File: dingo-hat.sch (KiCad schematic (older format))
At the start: 51 parts, among them J1 6-13V, J14 NEOPIXEL, J15 MPU-9250, J16 4, J17 5, J18 6, J19 7, J2 Raspberry_Pi_2_3, J24 3mm_Mount, J25 3mm_Mount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

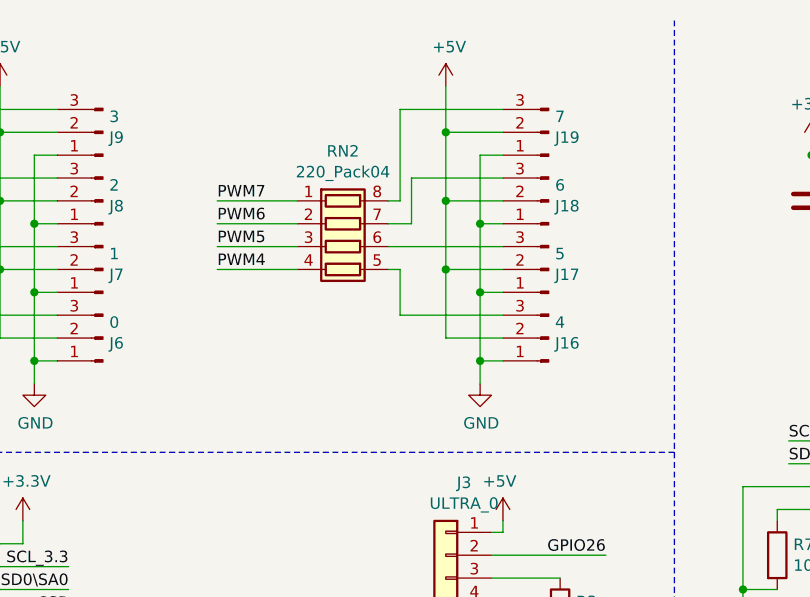
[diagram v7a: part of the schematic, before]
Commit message: Removed 4 of the Servo pins
We only need 4.
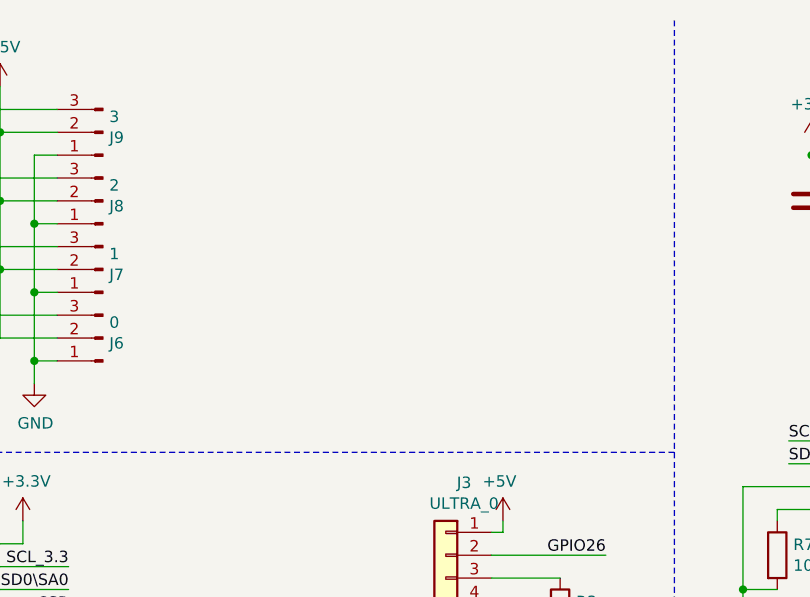
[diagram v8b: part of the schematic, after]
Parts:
- removed J16: 4, Connector_PinHeader_2.54mm:PinHeader_1x03_P2.54mm_Vertical, symbol Connector:Conn_01x03_Male
- removed J17: 5, Connector_PinHeader_2.54mm:PinHeader_1x03_P2.54mm_Vertical, symbol Connector:Conn_01x03_Male
- removed J18: 6, Connector_PinHeader_2.54mm:PinHeader_1x03_P2.54mm_Vertical, symbol Connector:Conn_01x03_Male
- removed J19: 7, Connector_PinHeader_2.54mm:PinHeader_1x03_P2.54mm_Vertical, symbol Connector:Conn_01x03_Male
- removed RN2: 220_Pack04, Resistor_SMD:R_Array_Convex_4x0603, symbol Device:R_Pack04
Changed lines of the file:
@@
 EESchema Schematic File Version 4
 LIBS:dingo-hat-cache
-EELAYER 30 0
+EELAYER 29 0
 EELAYER END
 $Descr A4 11693 8268
@@
 	5350 1000 5350 1300
 $Comp
-L Connector:Conn_01x03_Male J16
-U 1 1 5C067B2F
-P 7750 1900
-F 0 "J16" H 7722 1923 50  0000 R CNN
-F 1 "4" H 7722 1832 50  0000 R CNN
-F 2 "Connector_PinHeader_2.54mm:PinHeader_1x03_P2.54mm_Vertical" H 7750 1900 50  0001 C CNN
-F 3 "~" H 7750 1900 50  0001 C CNN
-	1    7750 1900
-	-1   0    0    1
-$EndComp
-$Comp
-L Device:R_Pack04 RN2
-U 1 1 5C067B35
-P 6850 1500
-F 0 "RN2" V 6433 1500 50  0000 C CNN
-F 1 "220_Pack04" V 6524 1500 50  0000 C CNN
-F 2 "Resistor_SMD:R_Array_Convex_4x0603" V 7125 1500 50  0001 C CNN
-F 3 "~" H 6850 1500 50  0001 C CNN
-F 4 "SMD" H 0   0   50  0001 C CNN "Package"
-	1    6850 1500
-	0    1    1    0
-$EndComp
-$Comp
-L Connector:Conn_01x03_Male J17
-U 1 1 5C067B3B
-P 7750 1600
-F 0 "J17" H 7722 1623 50  0000 R CNN
-F 1 "5" H 7722 1532 50  0000 R CNN
-F 2 "Connector_PinHeader_2.54mm:PinHeader_1x03_P2.54mm_Vertical" H 7750 1600 50  0001 C CNN
-F 3 "~" H 7750 1600 50  0001 C CNN
-	1    7750 1600
-	-1   0    0    1
-$EndComp
-$Comp
-L Connector:Conn_01x03_Male J18
-U 1 1 5C067B41
-P 7750 1300
-F 0 "J18" H 7722 1323 50  0000 R CNN
-F 1 "6" H 7722 1232 50  0000 R CNN
-F 2 "Connector_PinHeader_2.54mm:PinHeader_1x03_P2.54mm_Vertical" H 7750 1300 50  0001 C CNN
-F 3 "~" H 7750 1300 50  0001 C CNN
-	1    7750 1300
-	-1   0    0    1
-$EndComp
-$Comp
-L Connector:Conn_01x03_Male J19
-U 1 1 5C067B47
-P 7750 1000
-F 0 "J19" H 7722 1023 50  0000 R CNN
-F 1 "7" H 7722 932 50  0000 R CNN
-F 2 "Connector_PinHeader_2.54mm:PinHeader_1x03_P2.54mm_Vertical" H 7750 1000 50  0001 C CNN
-F 3 "~" H 7750 1000 50  0001 C CNN
-	1    7750 1000
-	-1   0    0    1
-$EndComp
-Wire Wire Line
-	7050 1300 7100 1300
-Wire Wire Line
-	7100 1300 7100 900
-Wire Wire Line
-	7100 900  7550 900
-Wire Wire Line
-	7050 1400 7150 1400
-Wire Wire Line
-	7150 1400 7150 1200
-Wire Wire Line
-	7150 1200 7550 1200
-Wire Wire Line
-	7050 1500 7550 1500
-Wire Wire Line
-	7050 1600 7100 1600
-Wire Wire Line
-	7100 1600 7100 1800
-Wire Wire Line
-	7100 1800 7550 1800
-$Comp
-L power:+5V #PWR0114
-U 1 1 5C067B5F
-P 7300 800
-F 0 "#PWR0114" H 7300 650 50  0001 C CNN
-F 1 "+5V" H 7315 973 50  0000 C CNN
-F 2 "" H 7300 800 50  0001 C CNN
-F 3 "" H 7300 800 50  0001 C CNN
-	1    7300 800
-	1    0    0    -1
-$EndComp
-$Comp
-L power:GND #PWR0115
-U 1 1 5C067B65
-P 7450 2100
-F 0 "#PWR0115" H 7450 1850 50  0001 C CNN
-F 1 "GND" H 7455 1927 50  0000 C CNN
-F 2 "" H 7450 2100 50  0001 C CNN
-F 3 "" H 7450 2100 50  0001 C CNN
-	1    7450 2100
-	1    0    0    -1
-$EndComp
-Wire Wire Line
-	7550 1100 7450 1100
-Wire Wire Line
-	7450 1100 7450 1400
-Wire Wire Line
-	7550 1400 7450 1400
-Connection ~ 7450 1400
-Wire Wire Line
-	7450 1400 7450 1700
-Wire Wire Line
-	7550 1700 7450 1700
-Connection ~ 7450 1700
-Wire Wire Line
-	7450 1700 7450 2000
-Wire Wire Line
-	7550 2000 7450 2000
-Connection ~ 7450 2000
-Wire Wire Line
-	7450 2000 7450 2100
-Wire Wire Line
-	7300 800  7300 1000
-Wire Wire Line
-	7300 1900 7550 1900
-Wire Wire Line
-	7300 1600 7550 1600
-Connection ~ 7300 1600
-Wire Wire Line
-	7300 1600 7300 1900
-Wire Wire Line
-	7550 1300 7300 1300
-Connection ~ 7300 1300
-Wire Wire Line
-	7300 1300 7300 1600
-Wire Wire Line
-	7550 1000 7300 1000
-Connection ~ 7300 1000
-Wire Wire Line
-	7300 1000 7300 1300
-Wire Wire Line
-	6650 1600 6300 1600
-Text Label 6300 1600 0    50   ~ 0
-PWM4
-Text Label 6300 1500 0    50   ~ 0
-PWM5
-Wire Wire Line
-	6650 1500 6300 1500
-Wire Wire Line
-	6650 1400 6300 1400
-Text Label 6300 1400 0    50   ~ 0
-PWM6
-Text Label 6300 1300 0    50   ~ 0
-PWM7
-Wire Wire Line
-	6650 1300 6300 1300
-$Comp
 L Device:LED D1
